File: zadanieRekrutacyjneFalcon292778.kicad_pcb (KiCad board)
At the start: 2 copper layers, 65 parts, among them J1 Conn_01x03_Pin, J2 Conn_01x02_Pin, J3 Conn_01x02_Pin, J4 Conn_01x04_Pin, J5 Conn_01x08_Pin, J6 Conn_01x08_Pin, J7 Conn_01x02_Pin, SW1 CK_KMS2xxG, SW2 SW_Nidec_CAS-120A1, SW3 CK_KMS2xxG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

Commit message: placement + testowy tracking v1
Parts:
- moved J5 73.7 mm to (159.4, 117.7), turned to -90 degrees
- moved U2 63.9 mm to (119.0, 84.1), turned to 90 degrees
- moved AE1 61.4 mm to (133.8, 93.8), turned to 90 degrees
- moved SW2 55.9 mm to (157.6, 106.0), turned to 180 degrees
- moved J7 52.7 mm to (167.0, 117.7), turned to -90 degrees
- moved J2 51.0 mm to (172.6, 117.5), turned to 90 degrees
- moved R1 50.9 mm to (179.9, 106.2), turned to 180 degrees
- moved C4 50.0 mm to (118.6, 97.5), turned to -90 degrees
- moved J1 48.4 mm to (131.2, 118.2), turned to 90 degrees
- moved R2 46.1 mm to (179.9, 102.6), turned to 180 degrees
- moved SW1 44.9 mm to (142.4, 105.5)
- moved J3 41.1 mm to (135.0, 58.2), turned to -90 degrees
- moved C13 37.6 mm to (170.8, 93.3), turned to 180 degrees
- moved R4 37.5 mm to (160.6, 108.5), turned to -90 degrees
- moved FB1 37.0 mm to (144.4, 71.4), turned to 180 degrees
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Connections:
- J4 pad 1: /JTAGMS -> /JTAGI
- J4 pad 4: /JTAGI -> /JTAGMS
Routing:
- net /BAJT1-0: track 0.00 -> 37.7 mm
- net /BAJT1-1: track 0.00 -> 36.1 mm
- net /BAJT1-2: track 0.00 -> 35.1 mm
- net /BAJT1-7: track 0.00 -> 34.7 mm
- net /BAJT1-3: track 0.00 -> 34.2 mm
- net /BAJT1-6: track 0.00 -> 34.0 mm
- net /USB+: track 0.00 -> 33.6 mm, vias 0 -> 2
- net /BAJT1-4: track 0.00 -> 33.3 mm
- net /USB-: track 0.00 -> 33.0 mm, vias 0 -> 2
- net /GPIO2: track 0.00 -> 33.0 mm
- net /BAJT1-5: track 0.00 -> 32.6 mm
- net /GPIO1: track 0.00 -> 32.3 mm
- net Net-(U1-CHIP_PU): track 0.00 -> 22.9 mm
- net /FLASH: track 0.00 -> 20.3 mm, vias 0 -> 2
- net /SPI1: track 0.00 -> 20.2 mm, vias 0 -> 2
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
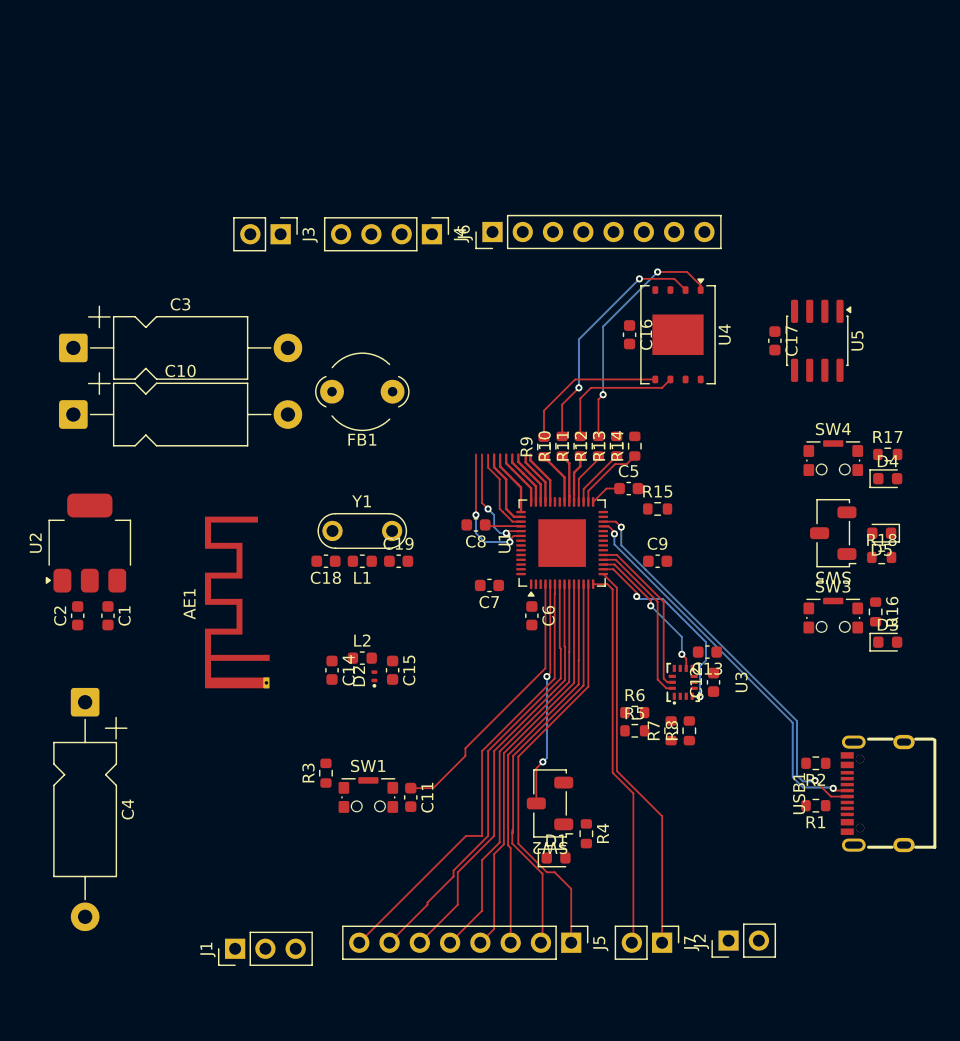
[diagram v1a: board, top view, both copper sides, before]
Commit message: zroutowane (do poprawy footprinty, DRC)
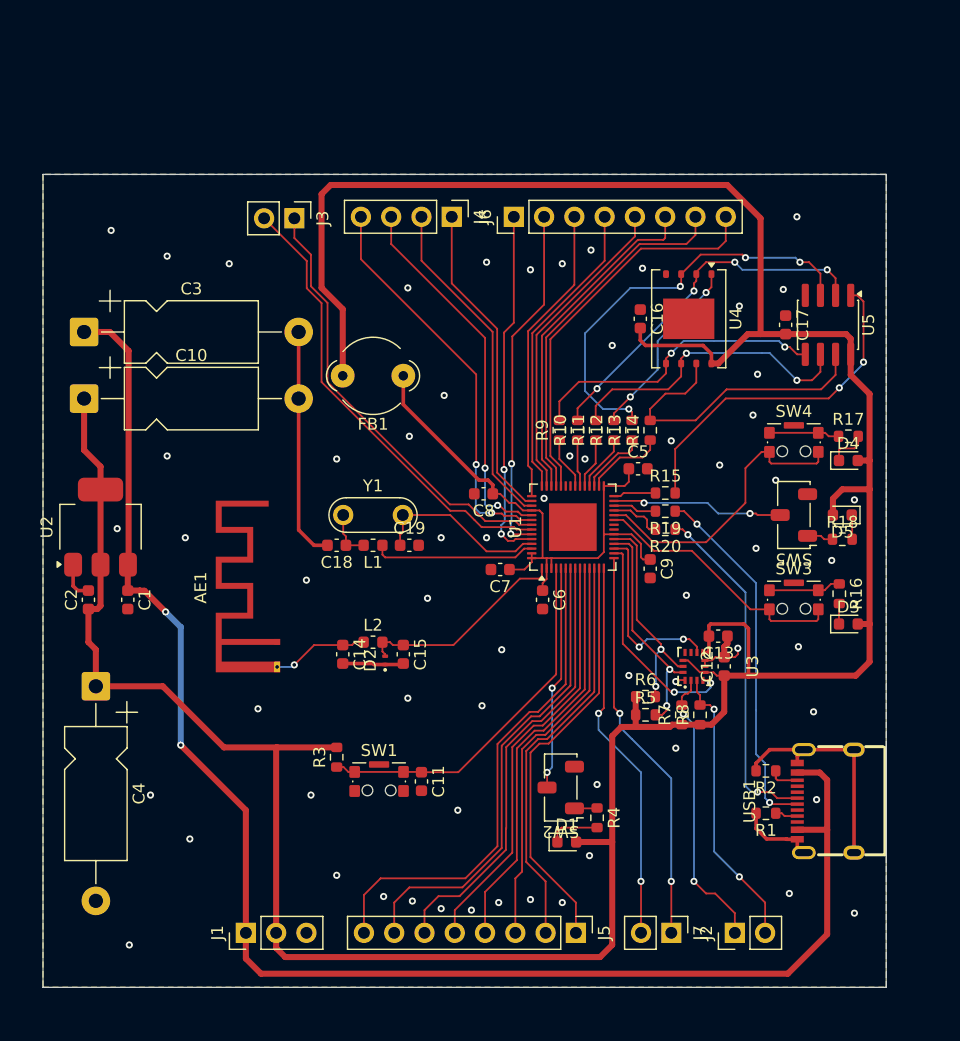
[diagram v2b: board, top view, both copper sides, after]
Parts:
- added R19: 33R, Resistor_SMD:R_0603_1608Metric, F.Cu at (167.3, 81.5)
- added R20: 33R, Resistor_SMD:R_0603_1608Metric, F.Cu at (167.3, 83.0)
- moved R1 4.24 mm to (175.7, 106.8)
- moved R2 4.24 mm to (175.7, 103.3)
- moved USB1 4.24 mm to (180.7, 105.8)
- moved D3 3.64 mm to (182.6, 90.9)
- moved D4 3.64 mm to (182.6, 77.2)
- moved D5 3.64 mm to (182.1, 81.8)
- moved R17 3.64 mm to (182.6, 75.2)
- moved R18 3.64 mm to (182.1, 83.8)
- moved SW3 3.64 mm to (178.1, 88.9)
- moved SW4 3.64 mm to (178.1, 75.7)
- moved SW5 3.64 mm to (178.1, 81.8)
- moved R16 3.41 mm to (181.9, 88.4)
- moved C8 2.68 mm to (152.0, 80.0)
- moved J4 2.21 mm to (149.4, 56.8)
- moved J6 2.20 mm to (154.6, 56.8)
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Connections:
- J4 pad 1: /JTAGI -> /JTAGCLK
- J4 pad 2: /JTAGCLK -> /JTAGO
- J4 pad 3: /JTAGO -> /JTAGI
- USB1 pad 6: /USB+ -> Net-(USB1-DP1)
- USB1 pad 7: /USB- -> Net-(USB1-DN1)
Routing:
- net +3.3V: track 0.00 -> 276.8 mm
- net VBUS: track 0.00 -> 129.2 mm, vias 0 -> 2
- net GND: track 0.00 -> 60.4 mm, vias 0 -> 63
- net VAnalog: track 5.73 -> 49.2 mm
- net /RXD: track 0.00 -> 38.5 mm
- net /TXD: track 0.00 -> 37.0 mm
- net /SPI2: track 0.00 -> 35.7 mm, vias 0 -> 4
- net Net-(USB1-DP1): track 0.00 -> 30.5 mm, vias 0 -> 2
- net /USB+: track 33.6 -> 3.67 mm, vias 2 -> 0
- net /BAJT2-7: track 0.00 -> 30.0 mm, vias 0 -> 2
- net /BAJT2-6: track 0.00 -> 29.8 mm, vias 0 -> 2
- net Net-(USB1-DN1): track 0.00 -> 29.1 mm, vias 0 -> 2
- net /PSRAM: track 0.00 -> 29.0 mm, vias 0 -> 2
- net /USB-: track 33.0 -> 4.51 mm, vias 2 -> 0
- net /BAJT2-0: track 4.67 -> 32.8 mm
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- added copper zone on B.Cu, net GND
- added copper zone on F.Cu, net GND
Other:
- board outline added: 70.7 x 68.2 mm

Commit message: DRC naprawione 3d modele dodane, transile dodane
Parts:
- added D6: ESD, Diode_SMD:D_SOD-523, F.Cu at (175.8, 105.0)
- added D7: ESD, Diode_SMD:D_SOD-523, F.Cu at (175.8, 106.6)
- moved R1 2.71 mm to (176.7, 109.3), turned to -90 degrees
- moved R2 1.59 mm to (176.7, 102.0), turned to 90 degrees
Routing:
- net GND: track 60.4 -> 30.6 mm, vias 63 -> 69
- net Net-(USB1-CC1): track 1.91 -> 2.78 mm
- net Net-(D7-K): track 30.5 -> 31.1 mm
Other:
- board text added: "Button1"
- board text added: "Button2"
- board text added: "Byte GPIO Bus"
- board text added: "ESP32-S3 BMI270 DevBoard"
- board text added: "Flash/Download mode toogle"
- board text added: "GPIO"
- board text added: "I2C"
- board text added: "JTAG"
- board text added: "Reset button"
- board text added: "Supply"
- board text added: "Switch1"
- board text added: "UART"

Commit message: Finalna wersja v1
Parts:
- moved D2 1.81 mm to (142.0, 94.1)
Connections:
- AE1 pad 2: (no net) -> GND
- D2 pad 2: /Wi-Fi -> Net-(AE1-A)
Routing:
- net Net-(AE1-A): track 8.12 -> 9.44 mm
- net /Wi-Fi: track 17.8 -> 16.5 mm
- net GND: track 30.6 -> 30.2 mm, vias 69 -> 73
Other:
- board size 70.7 x 68.2 mm -> 70.8 x 74.1 mm
- board text added: "+3.3V"
- board text added: "+5V"
- board text added: "CLK"
- board text added: "DATA"
- board text added: "GND"
- board text added: "I/O1"
- board text added: "I/O10"
- board text added: "I/O11"
- board text added: "I/O12"
- board text added: "I/O13"
- board text added: "I/O14"
- board text added: "I/O15"
- board text added: "I/O16"
- board text added: "I/O17"
- board text added: "I/O18"
- board text added: "I/O2"
- board text added: "I/O3"
- board text added: "I/O4"
- board text added: "I/O5"
- board text added: "I/O6"
- board text added: "I/O7"
- board text added: "I/O8"
- board text added: "I/O9"
- board text added: "IN"
- board text added: "OUT"
- board text added: "RXD"
- board text added: "TMS"
- board text added: "TXD"
